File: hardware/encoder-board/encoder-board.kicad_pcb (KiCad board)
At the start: 4 copper layers, 25.4 x 25.4 mm, 26 parts, among them J1 Conn_01x04, U1 ITR1204SR10A_TR(BY), U2 ITR1204SR10A_TR(BY), U3 LM2903

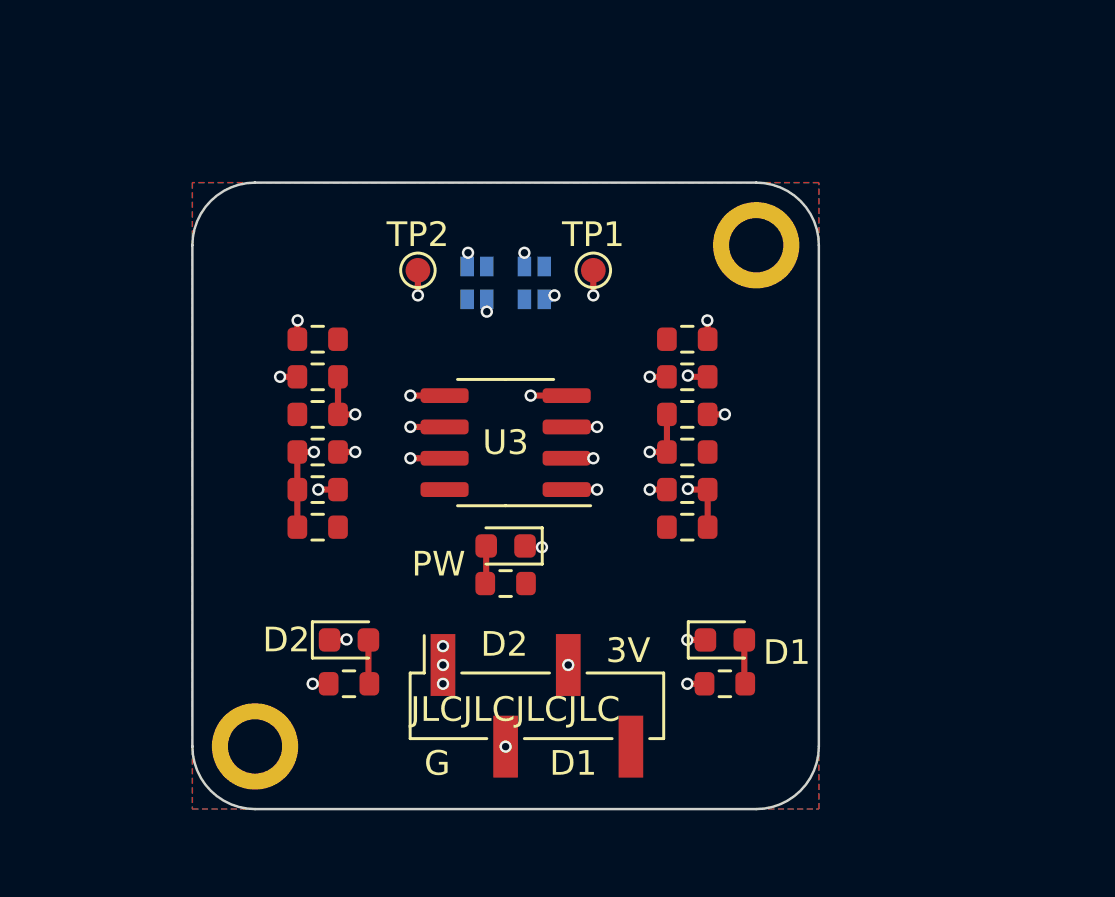
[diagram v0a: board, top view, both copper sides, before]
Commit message: fix encoder schematics. Prepare to redo pcb.
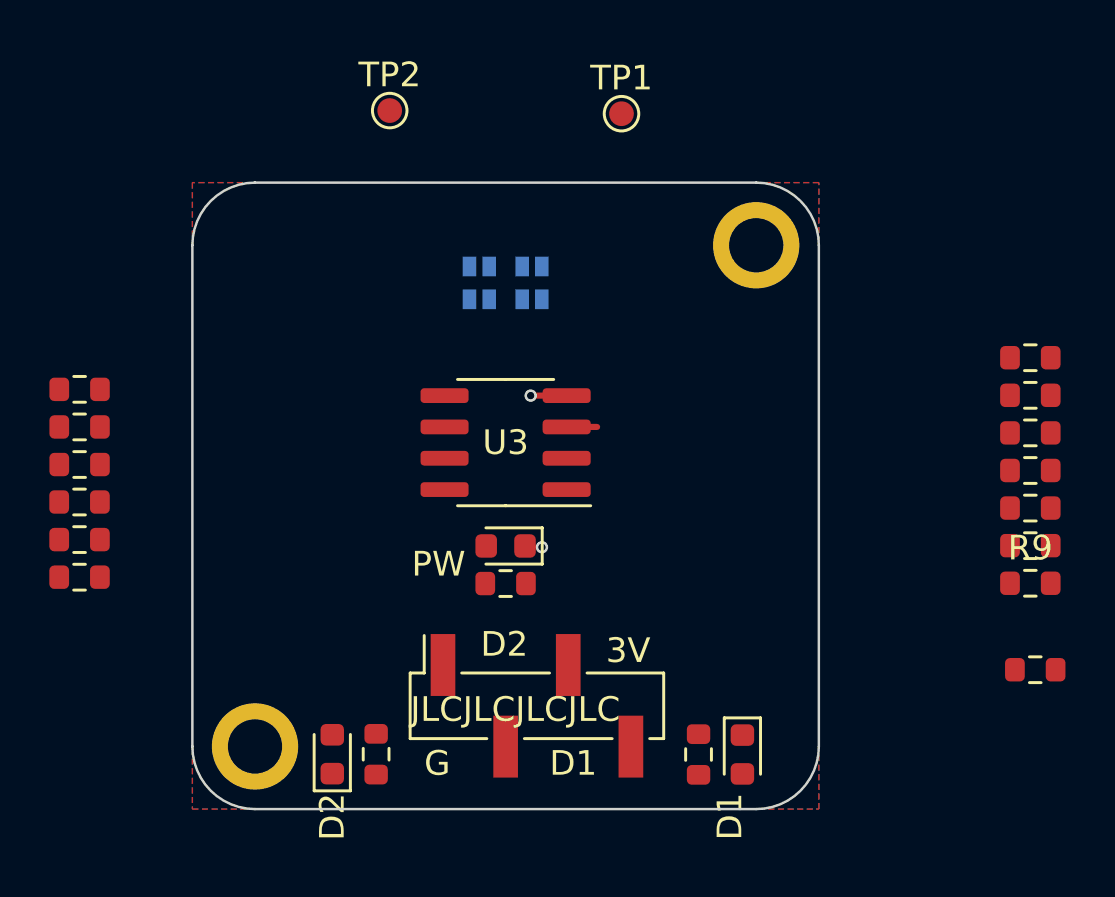
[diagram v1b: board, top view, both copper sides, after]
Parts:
- added R12: 100K, Resistor_SMD:R_0603_1608Metric, F.Cu at (59.6, 45.1)
- added R9: 100K, Resistor_SMD:R_0603_1608Metric, F.Cu at (59.4, 41.6)
- R1, R11, R14, R15, R2, R8: value 1k -> 10k
- R10, R13: value 1k -> 4.7k
- R3, R4: value 100 -> 220
- R5: value 30 -> 130
- moved R1 13.9 mm to (59.4, 40.1)
- moved R10 13.9 mm to (59.4, 38.6)
- moved R14 13.9 mm to (59.4, 35.5)
- moved R3 13.9 mm to (59.4, 32.5)
- moved R8 13.9 mm to (59.4, 37.1)
- moved R9 13.9 mm to (59.4, 34.0)
- moved R4 10.9 mm to (20.8, 36.8), turned to 180 degrees
- moved R13 9.87 mm to (20.8, 39.9)
- moved R2 9.87 mm to (20.8, 41.4)
- moved R12 9.87 mm to (20.8, 38.4)
- moved R11 9.67 mm to (20.8, 35.3)
- moved R15 9.67 mm to (20.8, 33.8)
- moved TP2 6.58 mm to (33.4, 22.5)
- moved TP1 6.45 mm to (42.8, 22.6)
- moved D1 4.70 mm to (47.7, 48.6), turned to -90 degrees
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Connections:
- R10 pad 1: D1 -> A1
- R10 pad 2: A1 -> +3V3
- R13 pad 1: D2 -> A2
- R13 pad 2: A2 -> +3V3
- U3 pad 1: D1 -> A1
- U3 pad 3: Net-(U3A-+) -> A1
- U3 pad 6: Net-(U3B--) -> A2
- U3 pad 7: D2 -> A2
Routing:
- net D2: track 24.0 -> 0.00 mm, vias 4 -> 0
- net A2: track 18.2 -> 0.00 mm, vias 3 -> 0
- net D1: track 17.6 -> 0.00 mm, vias 4 -> 0
- net A1: track 16.9 -> 1.23 mm, vias 4 -> 0
- net Net-(U2-A): track 10.4 -> 0.00 mm, vias 2 -> 0
- net Net-(U1-A): track 10.4 -> 0.00 mm, vias 2 -> 0
- net Net-(U3B-+): track 6.16 -> 0.00 mm, vias 2 -> 0
- net Net-(U3A--): track 5.70 -> 0.00 mm, vias 2 -> 0
- net Net-(U3A-+): track 4.91 -> 0.00 mm, vias 2 -> 0
- net Net-(U3B--): track 4.74 -> 0.00 mm, vias 2 -> 0
- net GND: track 4.30 -> 1.47 mm, vias 9 -> 2
- net Net-(D2-A): track 1.79 -> 0.00 mm
- net Net-(D1-A): track 1.79 -> 0.00 mm
- net Net-(PW1-A): track 1.54 -> 0.05 mm
